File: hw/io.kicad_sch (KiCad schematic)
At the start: 19 parts, among them J1 Conn_01x03_Pin, J19 Conn_01x02_Socket, J2 Conn_01x03_Pin, J3 DE9_Receptacle, J4 Conn_01x08_Socket, J5 Conn_01x02_Socket, J6 Conn_01x08_Socket, J7 Conn_01x02_Socket, J8 Conn_01x07_Socket, U10 W65C22NxP, U11 74HC138, U8 MC68B50, U9 MAX232

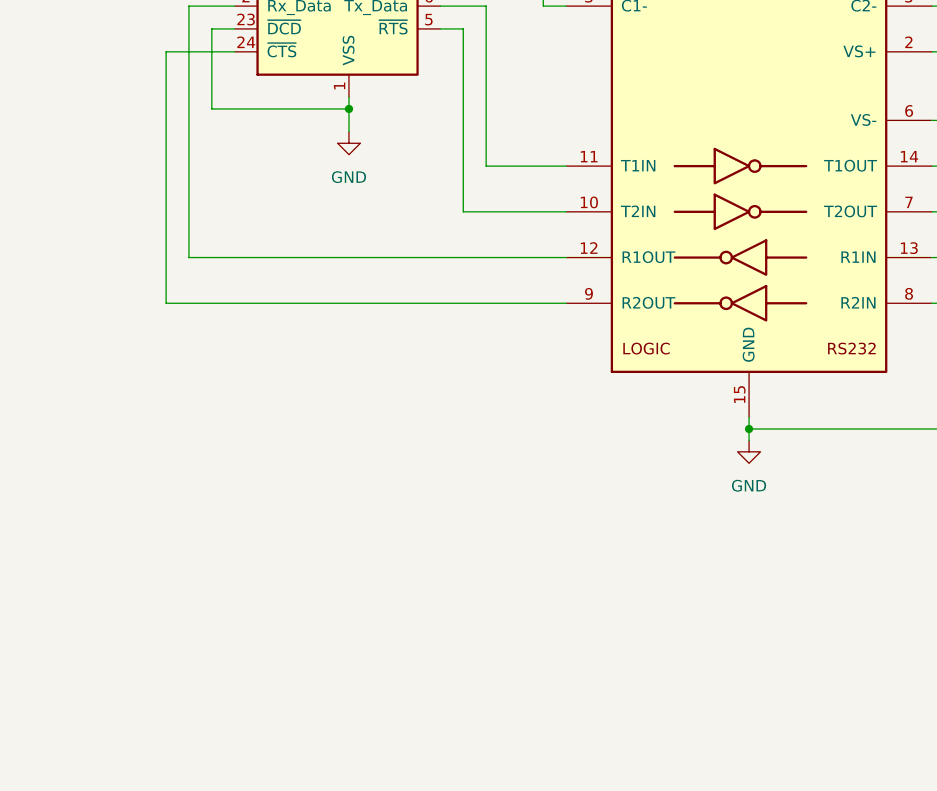
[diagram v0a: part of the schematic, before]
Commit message: additional pin sockets
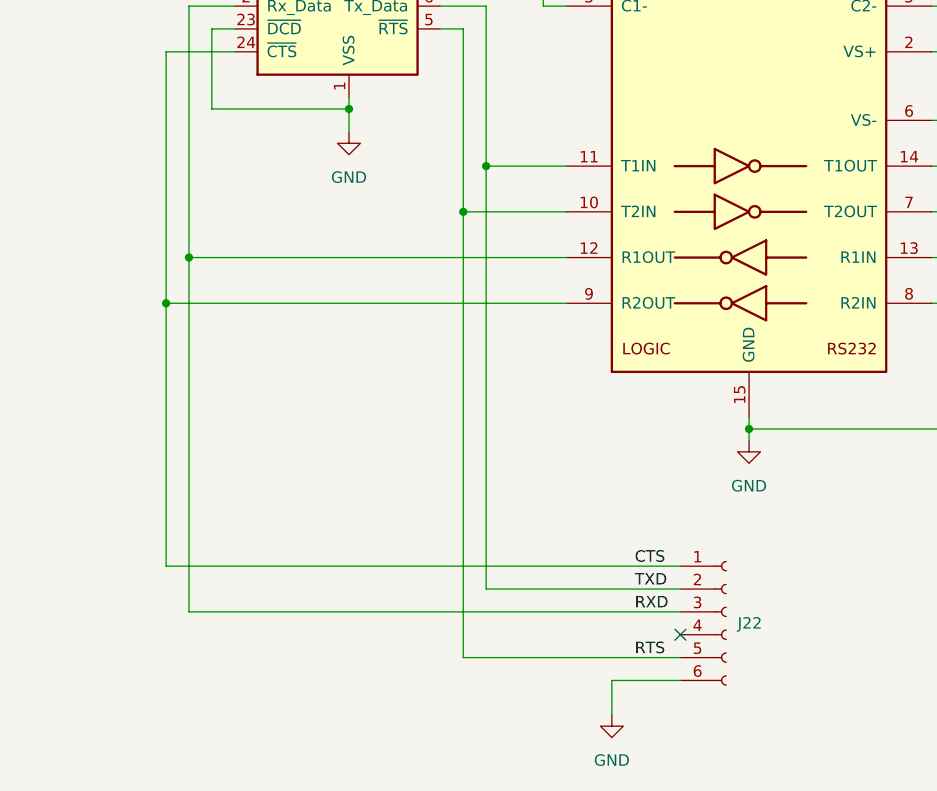
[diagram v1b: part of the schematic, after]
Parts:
- added J22: Conn_01x06_Socket, Connector_PinSocket_2.54mm:PinSocket_1x06_P2.54mm_Vertical, symbol Connector:Conn_01x06_Socket
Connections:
- net GND: now also J22.6 (Pin_6)
- net RTS: now reaches U8.5 (~{RTS}), U9.10 (T2IN)
- net RTS: now also J22.5 (Pin_5)
- net TXD: now reaches U8.6 (Tx_Data), U9.11 (T1IN)
- net TXD: now also J22.2 (Pin_2)
- net RXD: now reaches U8.2 (Rx_Data), U9.12 (R1OUT)
- net RXD: now also J22.3 (Pin_3)
- net CTS: now reaches U8.24 (~{CTS}), U9.9 (R2OUT)
- net CTS: now also J22.1 (Pin_1)
- no-connect marks 1 -> 2

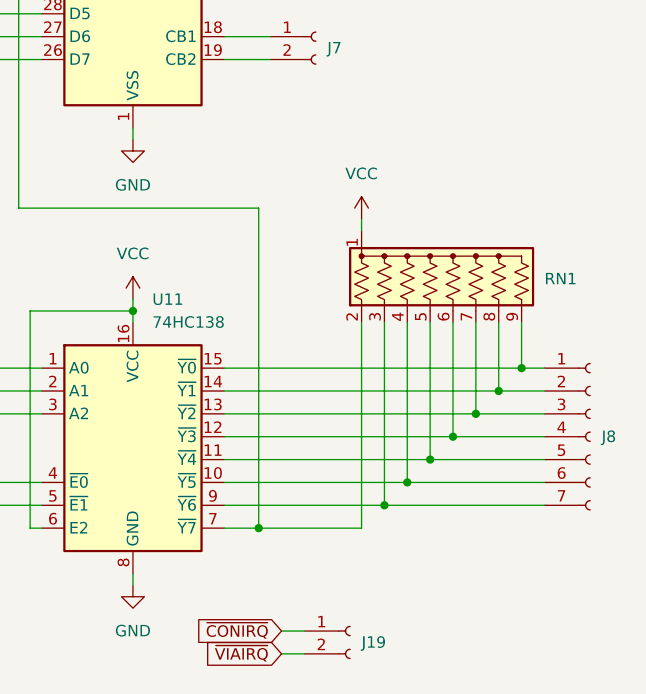
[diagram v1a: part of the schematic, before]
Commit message: remove unnecessary pullups
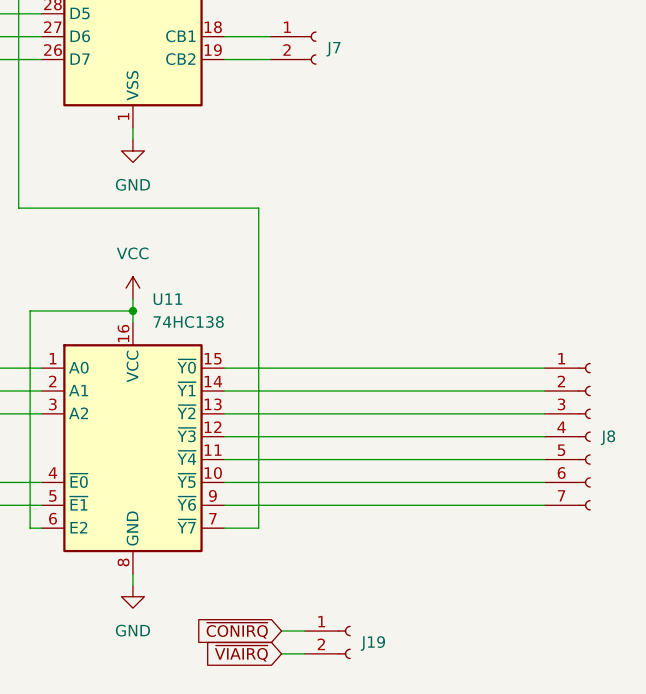
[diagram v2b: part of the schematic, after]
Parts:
- removed RN1: R_Network08_US, Resistor_THT:R_Array_SIP9, symbol Device:R_Network08_US
